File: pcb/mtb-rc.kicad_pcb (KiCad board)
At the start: 4 copper layers, 110 x 70 mm, 166 parts, among them J1 MVE252-5-V, J10 MVE252-5-V, J11 MVE252-5-V, J2 MVE252-5-V, J3 MVE252-5-V, J4 MVE252-5-V, J5 MVE252-5-V, J6 PINHEADER, J7 PINHEADER, J8 PROG/DEBUG, J9 MVE252-5-V, SW1 6x6, U1 VO0631T, U10 LM339, U11 LM339, U12 STM32F103C8Tx, U13 HT7533-1, U14 78M05, U15 MAX487, U2 VO0631T, U3 VO0631T, U4 L78L05_SOT89, U5 L79L05_SOT89, U6 LM339, U7 LM339, U8 LM339, U9 4052, Y1 14.7456MHz

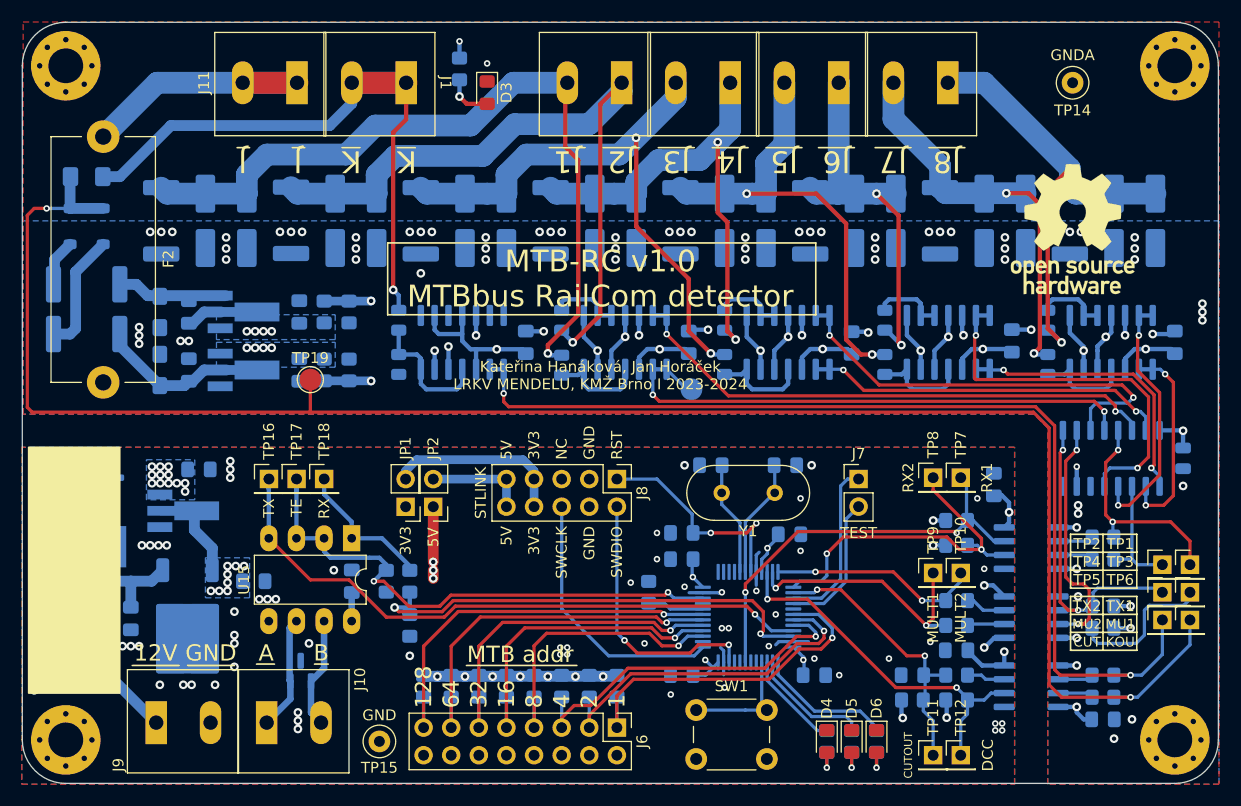
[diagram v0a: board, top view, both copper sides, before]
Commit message: w=11cm -> w=10cm.
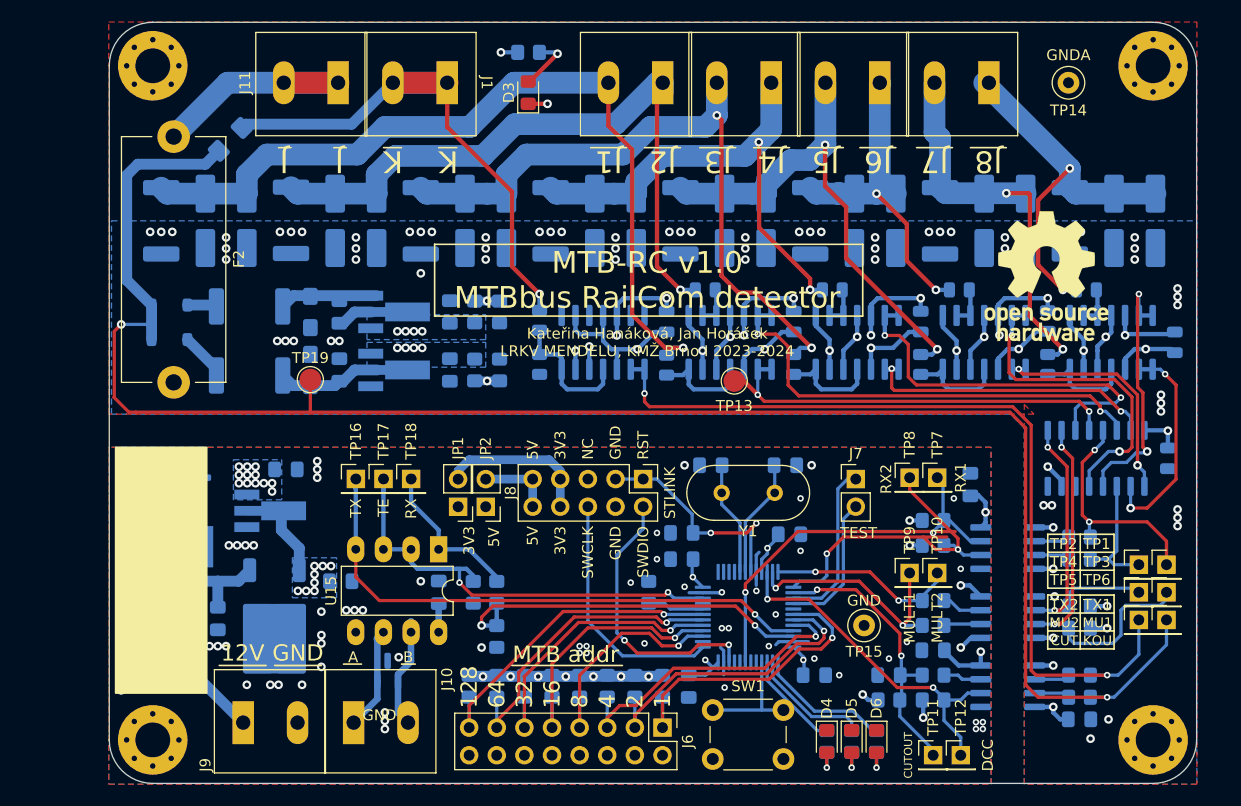
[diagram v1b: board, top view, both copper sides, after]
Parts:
- C11, C12, C14, C15, C16: footprint Capacitor_SMD:C_0805_2012Metric_Pad1.18x1.45mm_HandSolder -> Capacitor_SMD:C_0805_2012Metric
- TP13: moved to F.Cu
- moved TP15 45.8 mm to (177.4, 85.5)
- moved R19 15.5 mm to (120.9, 62.5)
- moved R18 15.1 mm to (120.9, 56.1)
- moved C5 13.8 mm to (126.5, 56.6)
- moved C6 13.8 mm to (126.5, 62.0)
- moved C10 13.8 mm to (139.3, 62.0)
- moved C7 13.8 mm to (129.2, 56.6)
- moved C8 13.8 mm to (129.2, 62.0)
- moved C9 13.8 mm to (139.3, 56.6)
- moved R24 13.8 mm to (141.6, 56.6)
- moved R25 13.8 mm to (143.9, 56.6)
- moved R26 13.8 mm to (143.9, 62.0)
- moved R27 13.8 mm to (141.6, 62.0)
- moved U4 13.8 mm to (134.5, 56.6)
- moved U5 13.8 mm to (134.5, 62.0)
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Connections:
- JP1 pad 1: +3V3 -> +5V
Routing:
- net -5VA: track 32.7 -> 50.2 mm, vias 15 -> 14
- net /DCC/CUTOUT: track 94.0 -> 78.9 mm
- net REF-: track 106.8 -> 93.1 mm
- net REF+: track 106.0 -> 93.1 mm
- net Net-(U9-X0): track 50.6 -> 39.2 mm
- net MTB-RX: track 43.6 -> 34.5 mm
- net K: track 59.2 -> 50.1 mm
- net MTB-TE: track 49.9 -> 41.0 mm
- net /DCC/J3: track 53.7 -> 62.3 mm
- net /DCC/J8: track 43.5 -> 35.6 mm
- net +5V: track 133.5 -> 125.6 mm, vias 13 -> 10
- net MTB-TX: track 58.3 -> 50.6 mm
- net Net-(U9-X1): track 50.2 -> 42.5 mm
- net ADDR-128: track 37.5 -> 30.1 mm
- net ADDR-64: track 35.0 -> 28.2 mm
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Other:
- board size 110 x 70 mm -> 100 x 70 mm

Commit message: Resolve DRC issues.
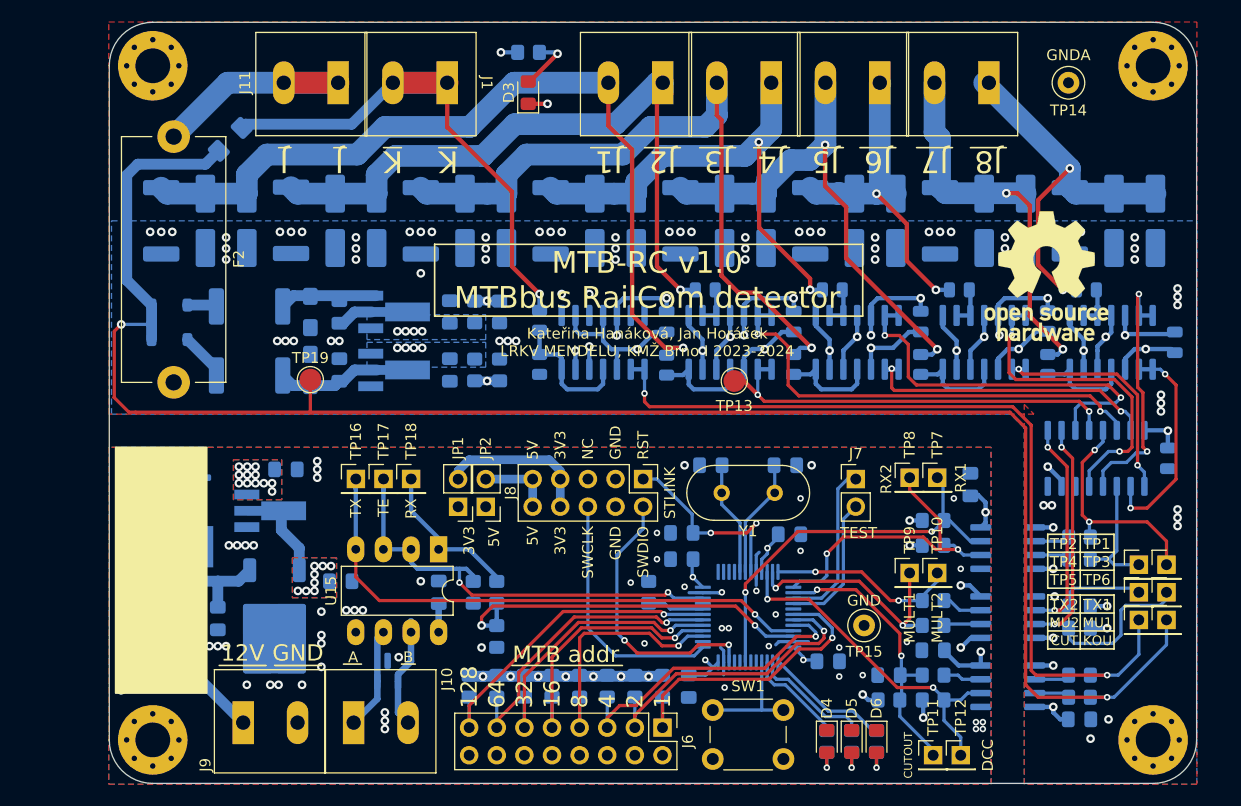
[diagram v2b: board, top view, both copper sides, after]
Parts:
- moved C19 1.80 mm to (174.1, 88.8)
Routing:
- net +5V: track 125.6 -> 120.3 mm
- net /DCC/J3: track 62.3 -> 65.3 mm, vias 2 -> 1
- net /MTB/RX2: track 33.2 -> 30.3 mm
- net RST: track 20.9 -> 18.5 mm
- net /MTB/RX1: track 38.6 -> 36.3 mm
- net ADDR-8: track 21.5 -> 23.5 mm
- net /BUS+: track 10.3 -> 9.45 mm
- net Net-(U12-PB12): track 12.4 -> 11.7 mm
- net /DCC/J7: track 37.3 -> 36.7 mm
- net GNDA: vias 69 -> 74
- net GND: vias 70 -> 66
- added copper zone on F.Cu, net +3V3
- added copper zone on F.Cu, net +5V
- added copper zone on In1.Cu, net +5V
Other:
- board text removed: "RX2 RX1"

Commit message: Minor tweaks.
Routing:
- net ADDR-1: track 28.6 -> 27.8 mm
- net /MTB/DCC: track 32.1 -> 32.9 mm
- net ADDR-2: track 28.3 -> 27.5 mm
- net ADDR-4: track 28.8 -> 28.1 mm

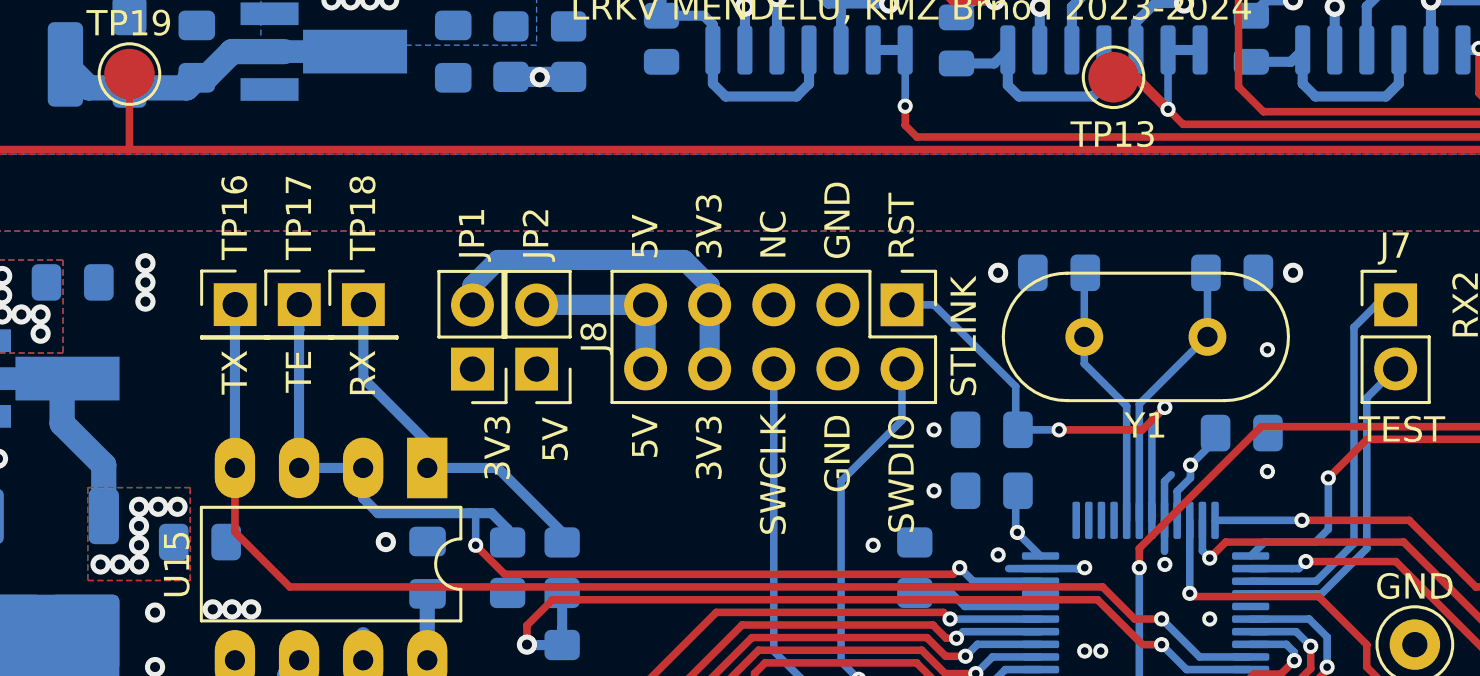
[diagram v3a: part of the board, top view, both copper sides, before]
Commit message: More space for STlink connector.
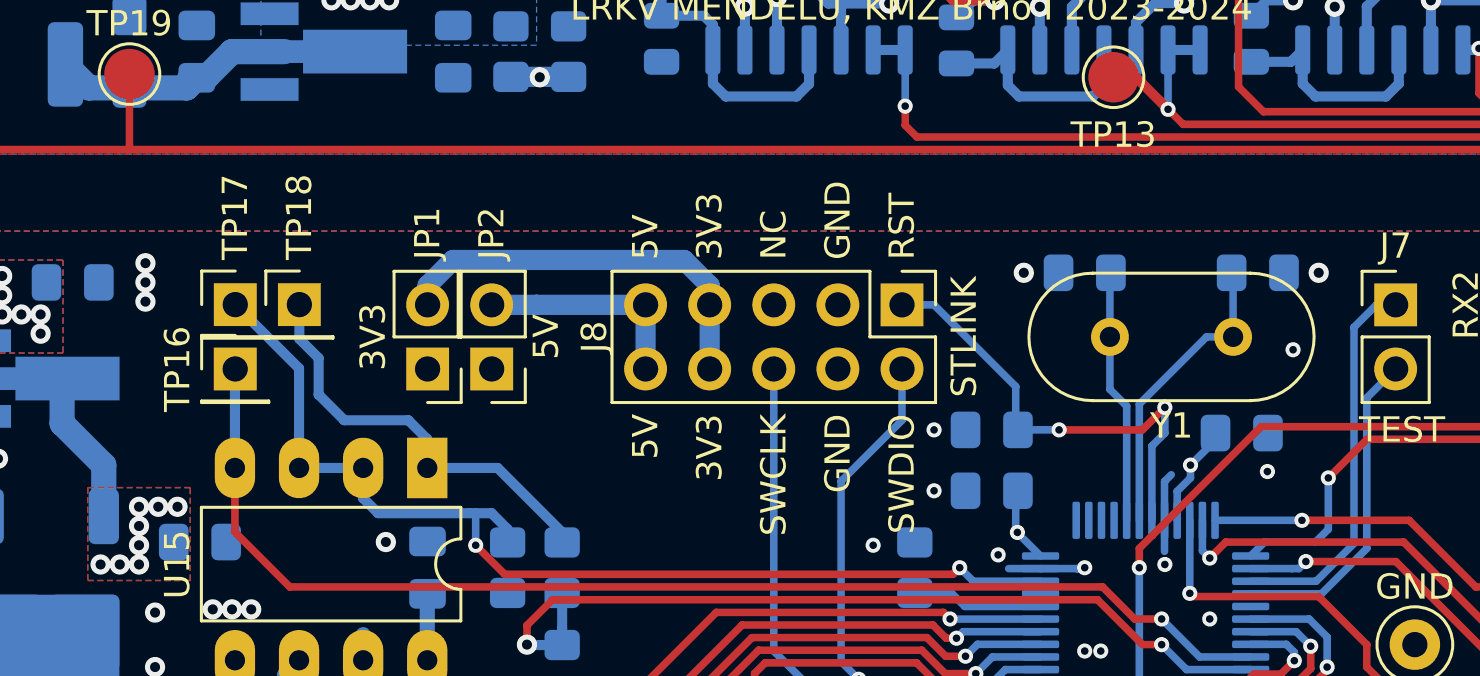
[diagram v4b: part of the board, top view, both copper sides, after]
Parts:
- moved TP16 2.55 mm to (130.7, 74.5)
- moved TP17 2.54 mm to (130.7, 72.0)
- moved TP18 2.54 mm to (133.2, 72.0)
- moved JP2 1.78 mm to (140.8, 74.5)
- moved JP1 1.78 mm to (138.3, 74.5)
- moved Y1 1.02 mm to (170.2, 73.3)
- moved C22 1.02 mm to (164.3, 70.7)
- moved C23 1.02 mm to (171.2, 70.7)
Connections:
- JP1 pad 1: +5V -> +3V3
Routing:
- net Net-(U15-R): track 14.3 -> 17.9 mm
- net MTB-TX: track 50.6 -> 48.8 mm
- net Net-(J8-Pin_10): track 6.87 -> 8.65 mm
- net Net-(J8-Pin_7): track 14.3 -> 16.1 mm
- net MTB-TE: track 41.0 -> 42.6 mm
- net Net-(U12-PD1): track 11.0 -> 12.0 mm
- net +5V: track 120.3 -> 119.7 mm

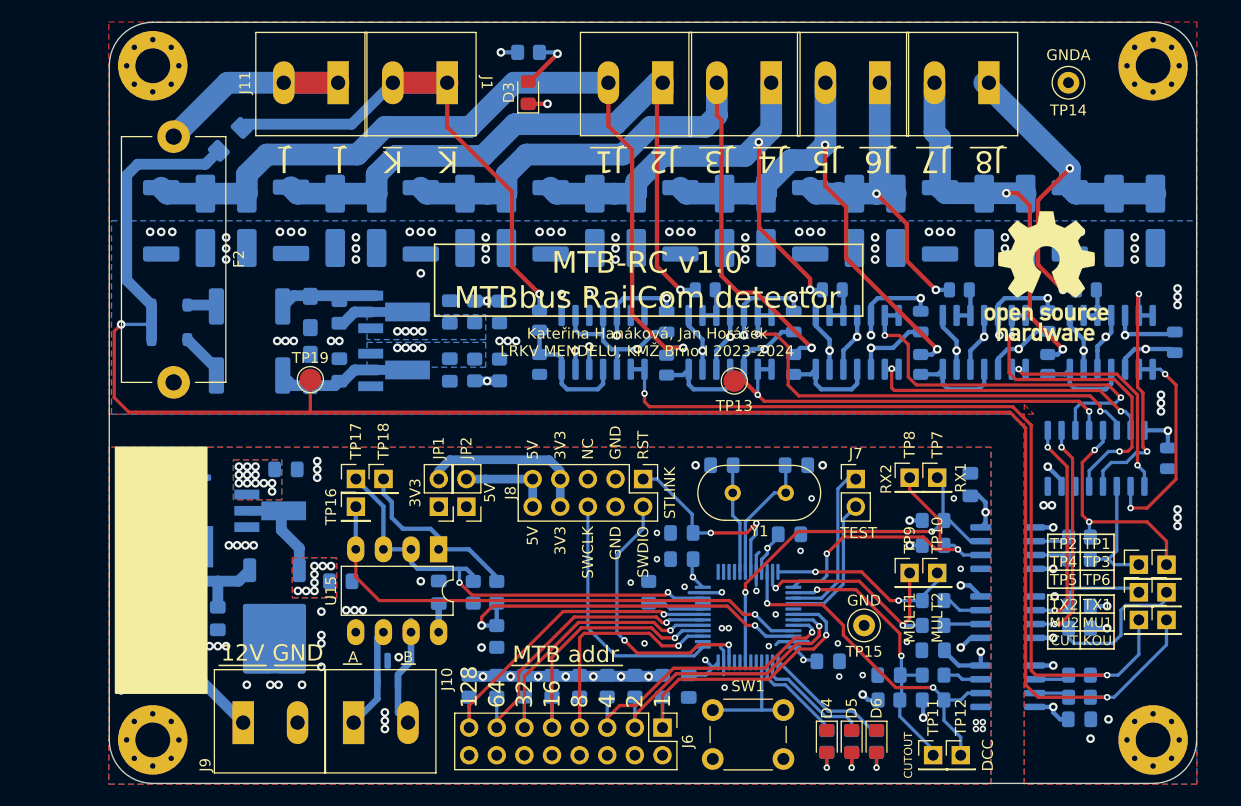
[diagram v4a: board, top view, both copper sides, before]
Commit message: Add explanatory texts.
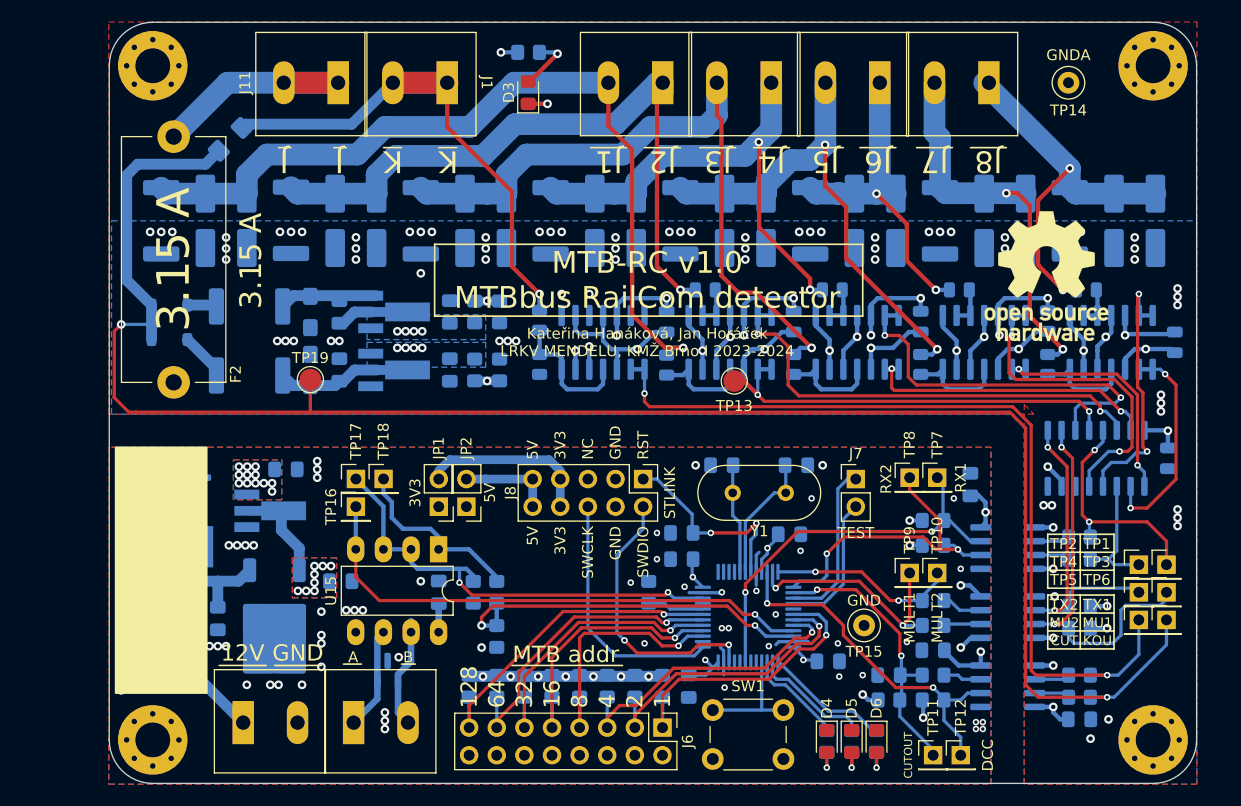
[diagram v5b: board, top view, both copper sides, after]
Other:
- board text added: "3.15 A"
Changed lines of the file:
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@@
     (property "ki_keywords" "screw terminal")
     (attr through_hole)
-    (fp_text reference "J9" (at -5.969 3.81 90 unlocked) (layer "F.SilkS")
+    (fp_text reference "J9" (at -5.969 3.81 90 unlocked) (layer "F.SilkS") hide
         (effects (font (size 1 1) (thickness 0.15)))
     )
@@
     (property "ki_keywords" "fuse")
     (attr through_hole)
-    (fp_text reference "F2" (at 11.25 -6 90) (layer "F.SilkS")
+    (fp_text reference "F2" (at 21.841 -5.715 90) (layer "F.SilkS")
         (effects (font (size 1 1) (thickness 0.15)))
     )
@@
     (property "ki_keywords" "screw terminal")
     (attr through_hole)
-    (fp_text reference "J10" (at 6.096 -4.064 90 unlocked) (layer "F.SilkS")
+    (fp_text reference "J10" (at 6.096 -4.064 90 unlocked) (layer "F.SilkS") hide
         (effects (font (size 1 1) (thickness 0.15)))
     )
@@
   (gr_line (start 207.01 89.9795) (end 200.914 89.9795)
     (stroke (width 0.15) (type default)) (layer "B.SilkS"))
-  (gr_line (start 176.784 88.9) (end 185.293 88.9)
+  (gr_line (start 176.784 88.9) (end 183.388 88.9)
     (stroke (width 0.15) (type default)) (layer "B.SilkS"))
   (gr_line (start 142.113 93.472) (end 142.748 92.837)
@@
   (gr_line (start 200.914 91.6305) (end 200.914 88.3285)
     (stroke (width 0.15) (type default)) (layer "B.SilkS"))
-  (gr_line (start 185.547 88.9) (end 185.955 89.308)
+  (gr_line (start 183.388 88.9) (end 183.796 89.308)
     (stroke (width 0.15) (type default)) (layer "B.SilkS"))
   (gr_line (start 207.01 86.6775) (end 207.01 91.6305)
@@
   (gr_line (start 200.914 88.3285) (end 200.914 86.6775)
     (stroke (width 0.15) (type default)) (layer "B.SilkS"))
-  (gr_line (start 185.293 88.9) (end 185.547 88.9)
-    (stroke (width 0.15) (type default)) (layer "B.SilkS"))
   (gr_line (start 124.714 41.529) (end 123.571 41.529)
     (stroke (width 0.15) (type default)) (layer "F.SilkS"))
@@
     (effects (font (size 1 1) (thickness 0.15)) (justify bottom mirror))
   )
+  (gr_text "3.15 A" (at 113.919 51.816 90) (layer "F.SilkS")
+    (effects (font (size 3 3) (thickness 0.25)))
+  )
   (gr_text "RX2" (at 179.451 72.009 90) (layer "F.SilkS")
     (effects (font (size 1 1) (thickness 0.15)))
@@
     (effects (font (size 2 2) (thickness 0.2)))
   )
-  (gr_text "TEST" (at 176.911 76.962) (layer "F.SilkS")
+  (gr_text "TEST" (at 176.657 76.962) (layer "F.SilkS")
     (effects (font (size 1 1) (thickness 0.15)))
   )
@@
     (effects (font (size 0.9 0.9) (thickness 0.15)))
   )
+  (gr_text "3.15 A" (at 121.031 51.943 90) (layer "F.SilkS")
+    (effects (font (size 2 2) (thickness 0.2)))
+  )
   (gr_text "J5" (at 173.863 42.799 180) (layer "F.SilkS")
